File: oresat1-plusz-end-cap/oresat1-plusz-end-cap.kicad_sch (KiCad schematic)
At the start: 38 parts, among them J1 M55-7011242R, J2 U.FL-R-SMA, U1 RM3100, U2 RM3100

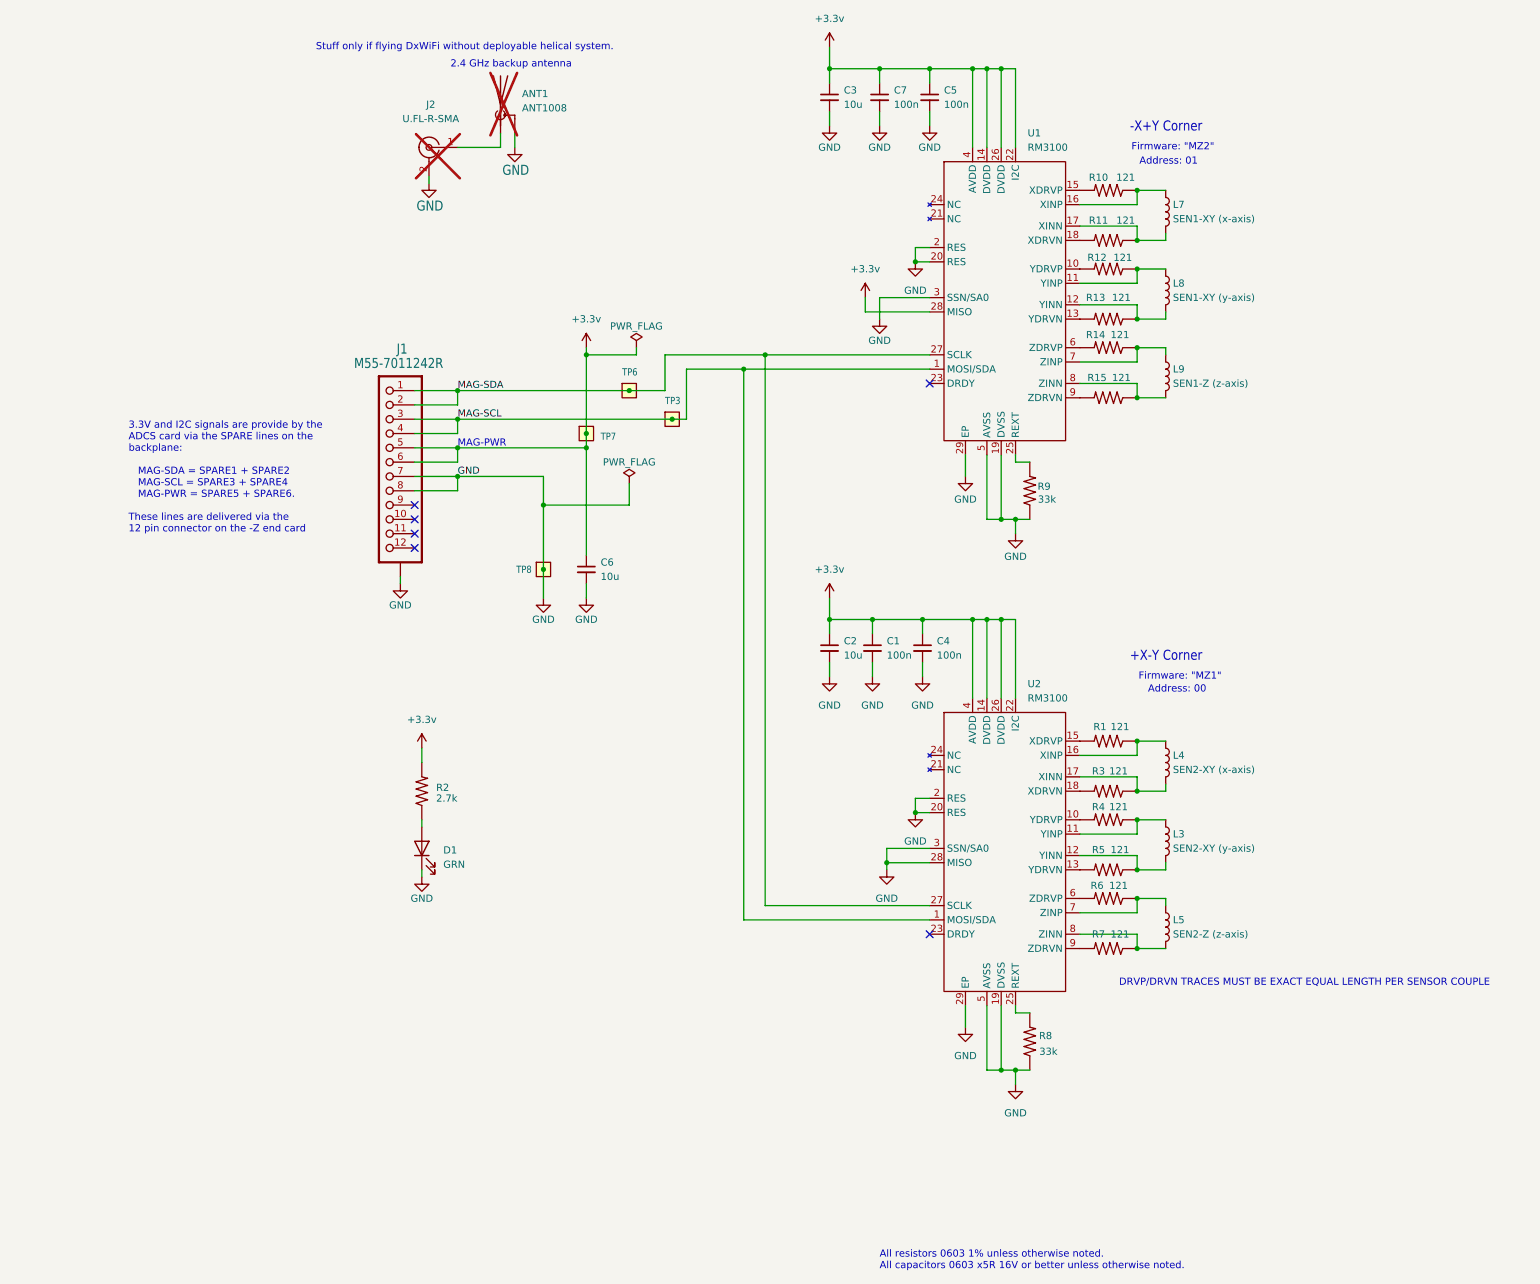
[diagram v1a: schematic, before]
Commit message: +Z End Cap ready for fab and assembly.
Schematic: Made RM3100 symbol better, cleaned up schematic, added variable strings, DRC'd,
added fiducials

Layout: Added fiducials, cleaned up polygons, rerouted signals too close to the edge,
Fixed the connector to the +Z End Card (it was wrong in so many ways), added all the
3D models to things, fixed the Makefile to use STEP not VRML files, reset the footprint
libraries Added the correct and latest DXF outline. Removed old DXF and old crusty
3D and other footprint files. Most important: ADDED KAOMOJI.

Makefile: Added flag to output STEP file with STP models, not VRML.
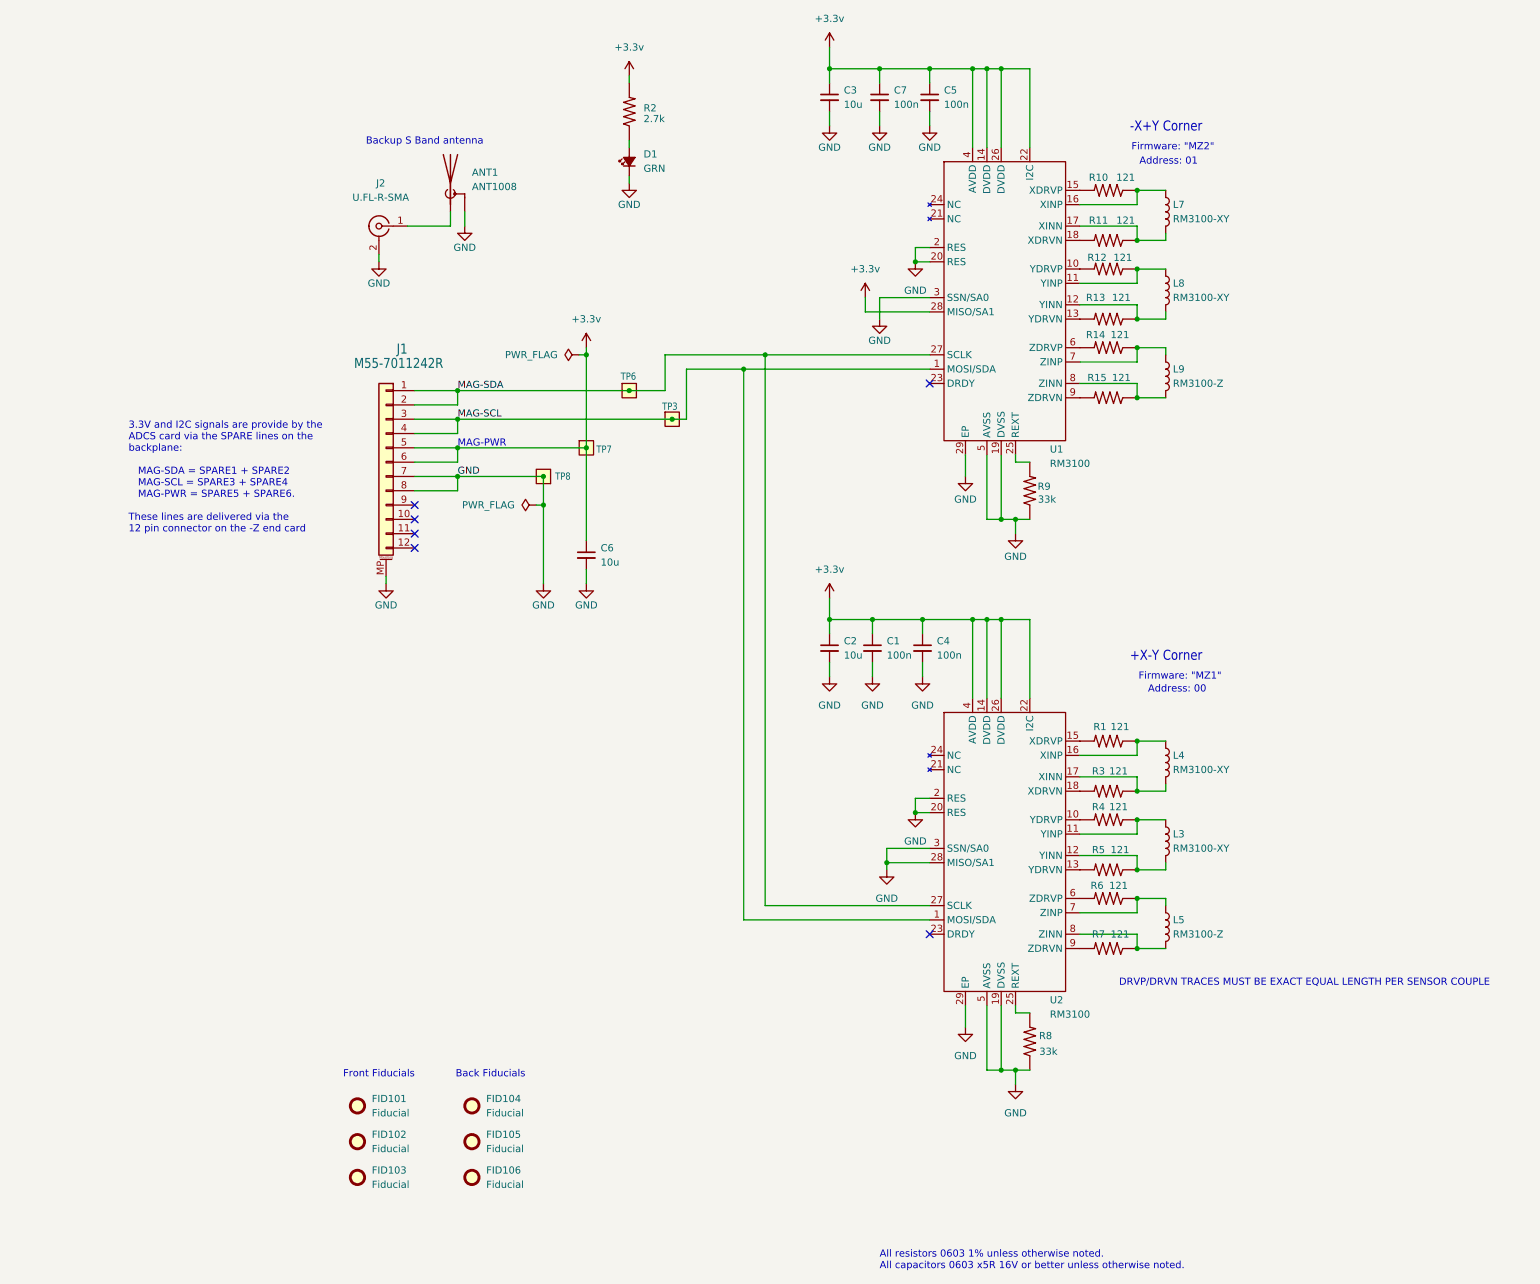
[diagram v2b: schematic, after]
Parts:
- added FID101, FID102, FID103, FID104, FID105, FID106: Fiducial, Fiducial:Fiducial_1mm_Mask2mm, symbol Mechanical:Fiducial
- ANT1: now fitted
- D1: footprint oresat-passives:0603-C-NOSILK -> LED_SMD:LED_0603_1608Metric; symbol Device:LED -> Device:LED_Small_Filled
- J1: footprint oresat-connectors:J-Harwin-M55-60X1242R -> oresat-connectors:J-Harwin-M55-7XX1242R; symbol oresat-connectors:J-HARWIN-M55-6001242R -> Connector_Generic_MountingPin:Conn_01x12_MountingPin
- J2: DST Digi-Key -> DigiKey; now fitted
- L3: value SEN2-XY (y-axis) -> RM3100-XY; DPN (none) -> N/A; DST (none) -> N/A; MFR (none) -> PNI Sensors; MPN (none) -> PN13104
- L4: value SEN2-XY (x-axis) -> RM3100-XY; DPN (none) -> N/A; DST (none) -> N/A; MFR (none) -> PNI Sensors; MPN (none) -> PN13104
- L5: value SEN2-Z (z-axis) -> RM3100-Z; DPN (none) -> N/A; DST (none) -> N/A; MFR (none) -> PNI Sensors; MPN (none) -> PN13101
- L7: value SEN1-XY (x-axis) -> RM3100-XY; DPN (none) -> N/A; DST (none) -> N/A; MFR (none) -> PNI Sensors; MPN (none) -> PN13104
- L8: value SEN1-XY (y-axis) -> RM3100-XY; DPN (none) -> N/A; DST (none) -> N/A; MFR (none) -> PNI Sensors; MPN (none) -> PN13104
- L9: value SEN1-Z (z-axis) -> RM3100-Z; DPN (none) -> N/A; DST (none) -> N/A; MFR (none) -> PNI Sensors; MPN (none) -> PN13101
- R1, R10, R11, R12, R13, R14, R15, R2, R3, R4, R5, R6, R7, R8, R9: DST (none) -> DigiKey
- U1, U2: DPN RM3100 -> N/A; DST (none) -> N/A; MFR (none) -> PNI Sensors; MPN (none) -> PN13156
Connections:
- net GND: now also J1.MP (MountPin); no longer J1.SH (SHIELD)
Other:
- note added: "Back Fiducials"
- note added: "Backup S Band antenna"
- note added: "Front Fiducials"
- note removed: "2.4 GHz backup antenna"
- note removed: "Stuff only if flying DxWiFi without deployable helical system."
- company: (none) -> Portland State Aerospace Society
- title: OreSat0.5 +Z End Cap -> OreSat1 +Z End Cap
- moved on the sheet: C6, R2, TP7, TP8

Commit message: Better doc notes, including on U.FL to U.FL cabling
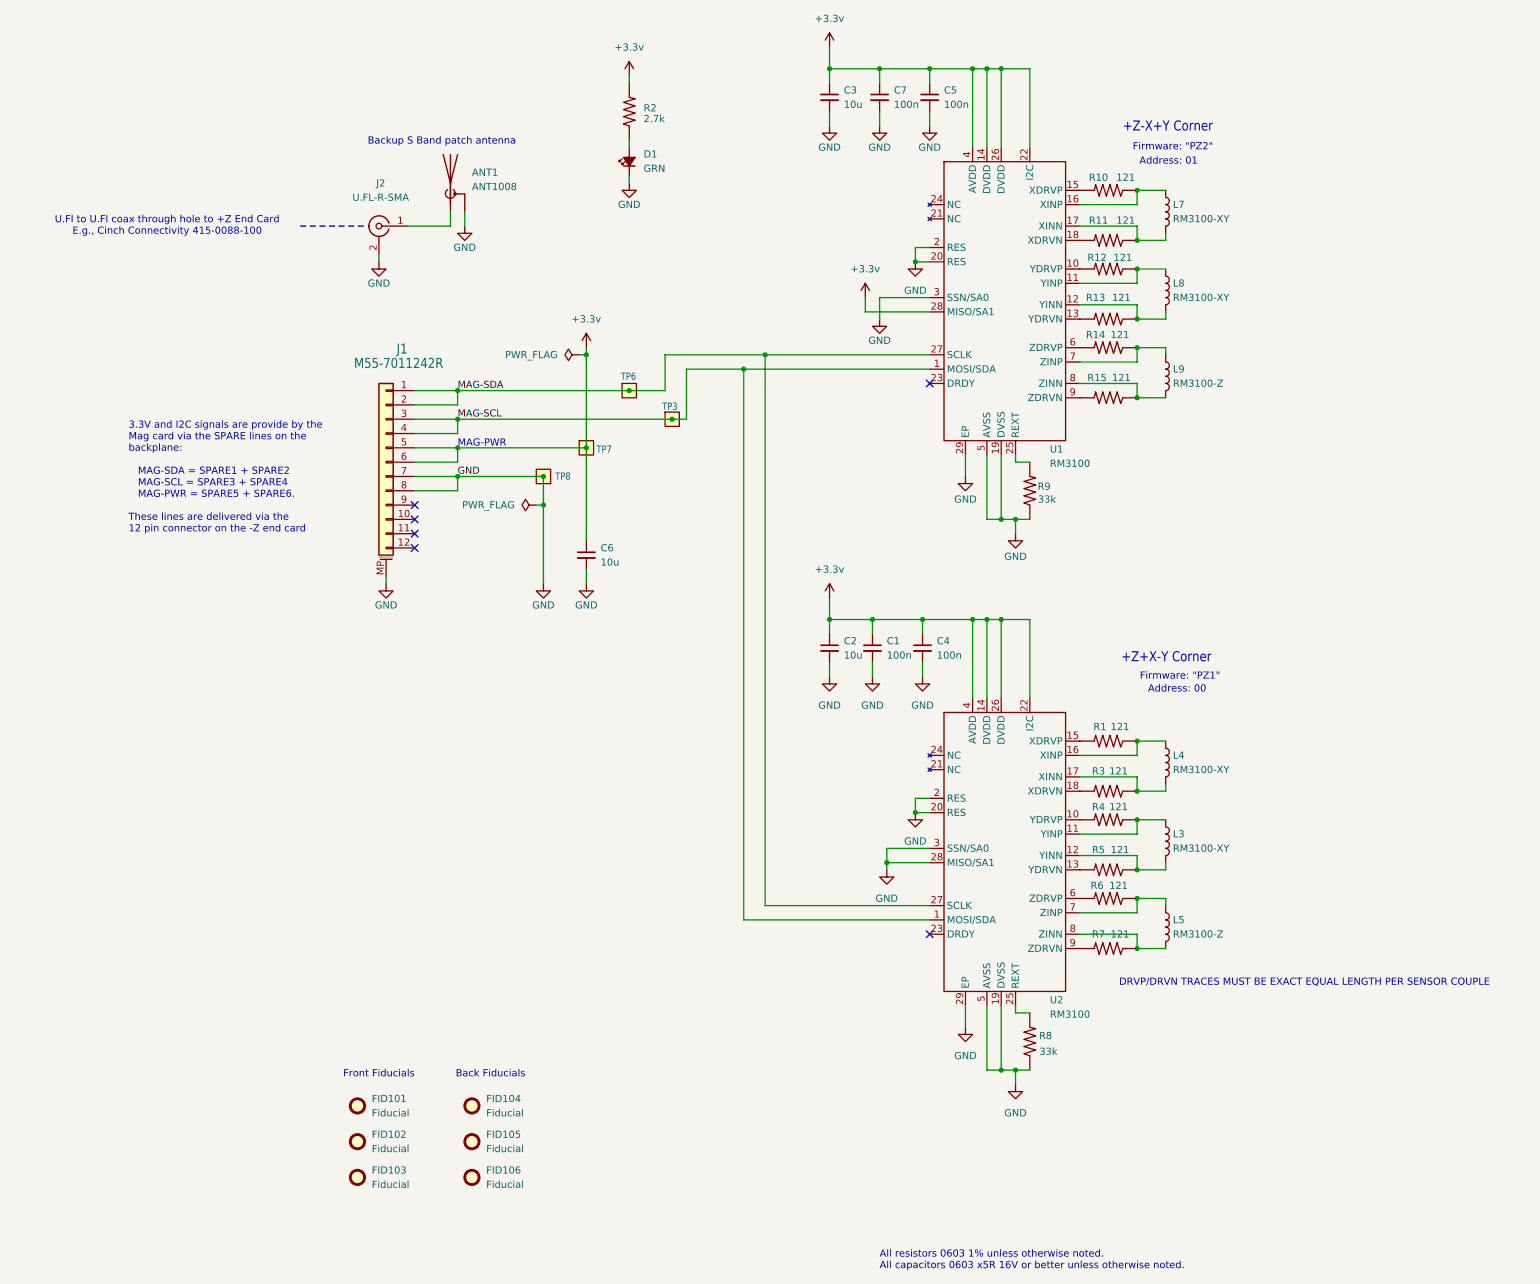
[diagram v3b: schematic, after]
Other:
- note added: "+Z+X-Y Corner"
- note added: "+Z-X+Y Corner"
- note added: "3.3V and I2C signals are provide by the Mag card via the SPARE lines on the backplane: MAG-SDA = SPARE1 + SPARE2 MAG-SCL = SPARE3 + SPARE4 MAG-PWR = SPARE5 + SPARE6. These lines are delivered via the 12 pin connector on the -Z end card"
- note added: "Backup S Band patch antenna"
- note added: "Firmware: "PZ1""
- note added: "Firmware: "PZ2""
- note added: "U.Fl to U.Fl coax through hole to +Z End Card E.g., Cinch Connectivity 415-0088-100"
- note removed: "+X-Y Corner"
- note removed: "-X+Y Corner"
- note removed: "3.3V and I2C signals are provide by the ADCS card via the SPARE lines on the backplane: MAG-SDA = SPARE1 + SPARE2 MAG-SCL = SPARE3 + SPARE4 MAG-PWR = SPARE5 + SPARE6. These lines are delivered via the 12 pin connector on the -Z end card"
- note removed: "Backup S Band antenna"
- note removed: "Firmware: "MZ1""
- note removed: "Firmware: "MZ2""
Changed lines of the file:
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@@
 		(company "Portland State Aerospace Society")
 	)
-	(text "Firmware: \"MZ2\""
+	(text "Firmware: \"PZ2\""
 		(exclude_from_sim no)
 		(at 289.56 62.23 0)
@@
 		)
 	)
-	(text "-X+Y Corner"
-		(exclude_from_sim no)
-		(at 281.94 59.69 0)
+	(text "+Z-X+Y Corner"
+		(exclude_from_sim no)
+		(at 280.67 59.69 0)
 		(effects
 			(font
@@
 		)
 	)
+	(text "U.Fl to U.Fl coax through hole to +Z End Card\nE.g., Cinch Connectivity 415-0088-100\n"
+		(exclude_from_sim no)
+		(at 110.998 76.2 0)
+		(effects
+			(font
+				(size 1.27 1.27)
+			)
+			(href "https://www.cinch.com/media/drawings/products/rf-microwave/cable-assemblies/cable-assembly/dr-ccs-john-415-0088-150.pdf")
+		)
+	)
 	(text "Front Fiducials"
 		(exclude_from_sim no)
@@
 		)
 	)
-	(text "3.3V and I2C signals are provide by the \nADCS card via the SPARE lines on the \nbackplane:\n\n   MAG-SDA = SPARE1 + SPARE2\n   MAG-SCL = SPARE3 + SPARE4 \n   MAG-PWR = SPARE5 + SPARE6.\n\nThese lines are delivered via the \n12 pin connector on the -Z end card"
+	(text "3.3V and I2C signals are provide by the \nMag card via the SPARE lines on the \nbackplane:\n\n   MAG-SDA = SPARE1 + SPARE2\n   MAG-SCL = SPARE3 + SPARE4 \n   MAG-PWR = SPARE5 + SPARE6.\n\nThese lines are delivered via the \n12 pin connector on the -Z end card"
 		(exclude_from_sim no)
 		(at 104.14 130.81 0)
@@
 		)
 	)
-	(text "Firmware: \"MZ1\""
+	(text "Firmware: \"PZ1\""
 		(exclude_from_sim no)
 		(at 290.83 156.21 0)
@@
 		)
 	)
-	(text "+X-Y Corner"
-		(exclude_from_sim no)
-		(at 281.94 153.67 0)
+	(text "+Z+X-Y Corner"
+		(exclude_from_sim no)
+		(at 280.416 153.924 0)
 		(effects
 			(font
@@
 		)
 	)
-	(text "Backup S Band antenna"
-		(exclude_from_sim no)
-		(at 156.718 61.214 0)
+	(text "Backup S Band patch antenna"
+		(exclude_from_sim no)
+		(at 159.766 61.214 0)
 		(effects
 			(font
@@
 		)
 	)
+	(polyline
+		(pts
+			(xy 134.62 76.2) (xy 146.05 76.2)
+		)
+		(stroke
+			(width 0)
+			(type dash)
+		)
+	)
